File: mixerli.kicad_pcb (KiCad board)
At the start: 2 copper layers, 126 x 108 mm, 166 parts, among them J1 QingPu_WQP-PJ366ST, J10 CONN_01X02, J11 CONN_01X02, J2 QingPu_WQP-PJ366ST, J3 QingPu_WQP-PJ366ST, J4 QingPu_WQP-PJ366ST, J5 QingPu_WQP-PJ366ST, J6 QingPu_WQP-PJ366ST, J7 QingPu_WQP-PJ366ST, J8 UJC-HP-3-SMT-TR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

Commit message: backups, move 3d stuff
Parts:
- removed G***: LOGO, stahllabs:LOGO_SGMK_Stamp_8.8mm
- removed REF**: OSHW-Logo2_7.3x6mm_SilkScreen, Symbol:OSHW-Logo2_7.3x6mm_SilkScreen
- D1, D3: footprint LEDs:LED_D3.0mm -> LED_THT:LED_Rectangular_W5.0mm_H2.0mm
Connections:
- H1 pad 1: GND -> unconnected-(H1-Pad1)
- H2 pad 1: GND -> unconnected-(H2-Pad1)
- H3 pad 1: GND -> unconnected-(H3-Pad1)
- H4 pad 1: GND -> unconnected-(H4-Pad1)
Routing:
- net unconnected-(H4-Pad1): track 0.00 -> 2.45 mm
- net GND: track 89.8 -> 87.3 mm

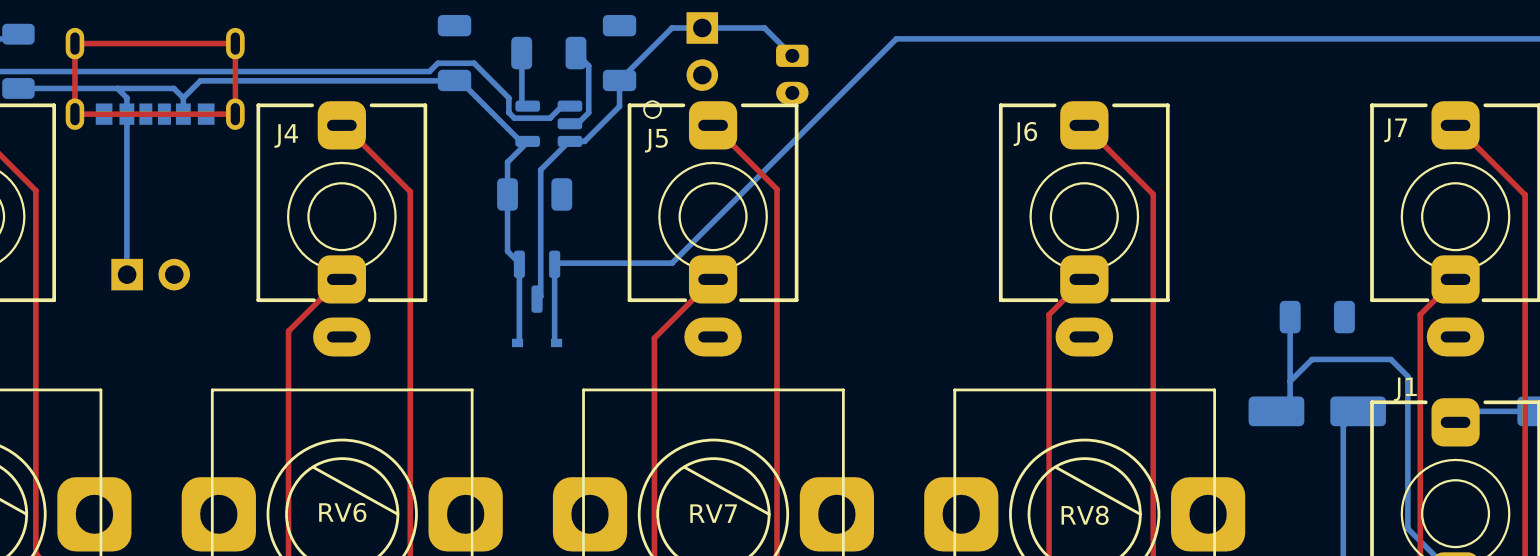
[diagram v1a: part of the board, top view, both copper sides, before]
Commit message: v2.0.1: fixed pulldown resistors
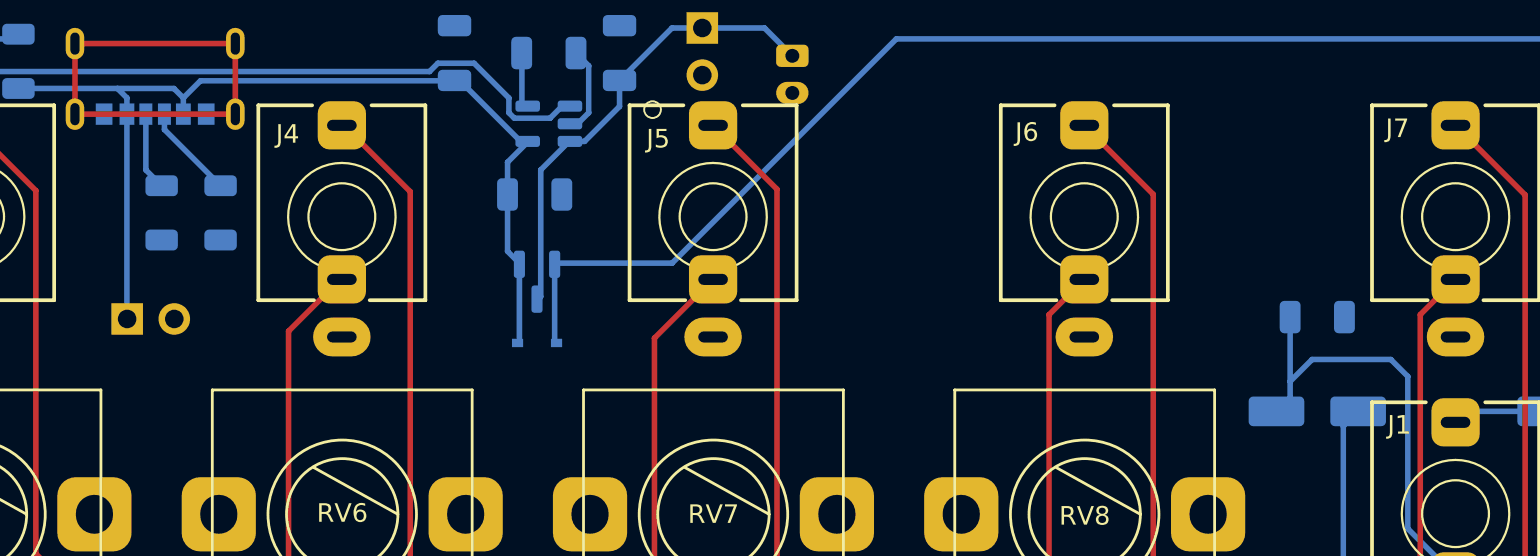
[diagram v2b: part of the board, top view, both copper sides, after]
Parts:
- added R68: 5.1k, Resistor_SMD:R_1206_3216Metric, B.Cu at (117.8, 47.4)
- added R69: 5.1k, Resistor_SMD:R_1206_3216Metric, B.Cu at (114.7, 47.4)
- J10, J11: value CONN_01X02 -> Battery
- moved J9 2.39 mm to (112.8, 53.1)
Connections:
- J8 pad A5: unconnected-(J8-CC1-PadA5) -> Net-(J8-CC1)
- J8 pad B5: unconnected-(J8-CC2-PadB5) -> Net-(J8-CC2)
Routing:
- net unconnected-(J8-SHIELD-PadS1)_2: track 24.9 -> 0.00 mm
- net unconnected-(J8-SHIELD-PadS1): track 0.00 -> 24.9 mm
- net Net-(J8-CC2): track 0.00 -> 5.11 mm
- net Net-(J8-CC1): track 0.00 -> 4.21 mm
- net /Power Supply/5V: track 51.9 -> 54.3 mm
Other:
- board text added: "v2.0.1 github.com/stahlnow/mixerli"
- board text removed: "v2.0.0 github.com/stahlnow/mixerli"
